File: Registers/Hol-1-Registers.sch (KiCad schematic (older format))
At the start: 26 parts, among them P1 DATA BUS, P2 REG-A-CTRL, P3 REG-B-CTRL, P4 REG-C-CTRL, P5 POWER, P6 CTRL-ALL, P7 REGISTER A LINK, P8 REGISTER B LINK, U1 74LS245, U2 74LS245, U3 74LS245, U4 74LS173, U5 74LS173, U6 74LS173, U7 74LS173, U8 74LS173, U9 74LS173

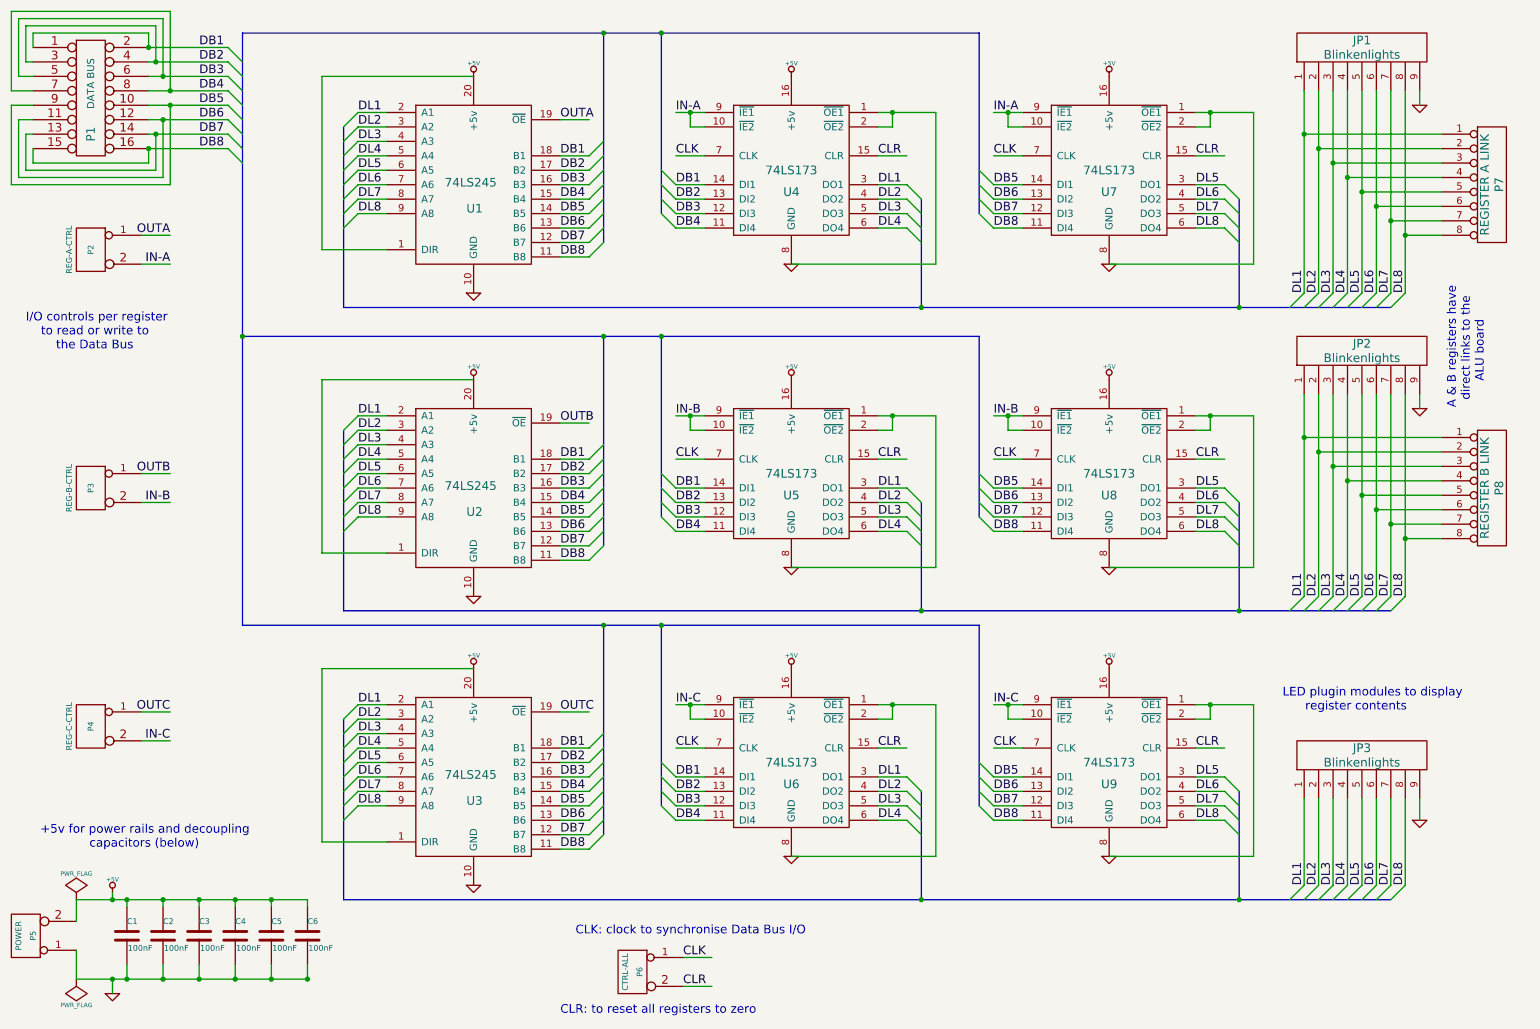
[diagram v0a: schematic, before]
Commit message: v1.3.2 corrected register net names
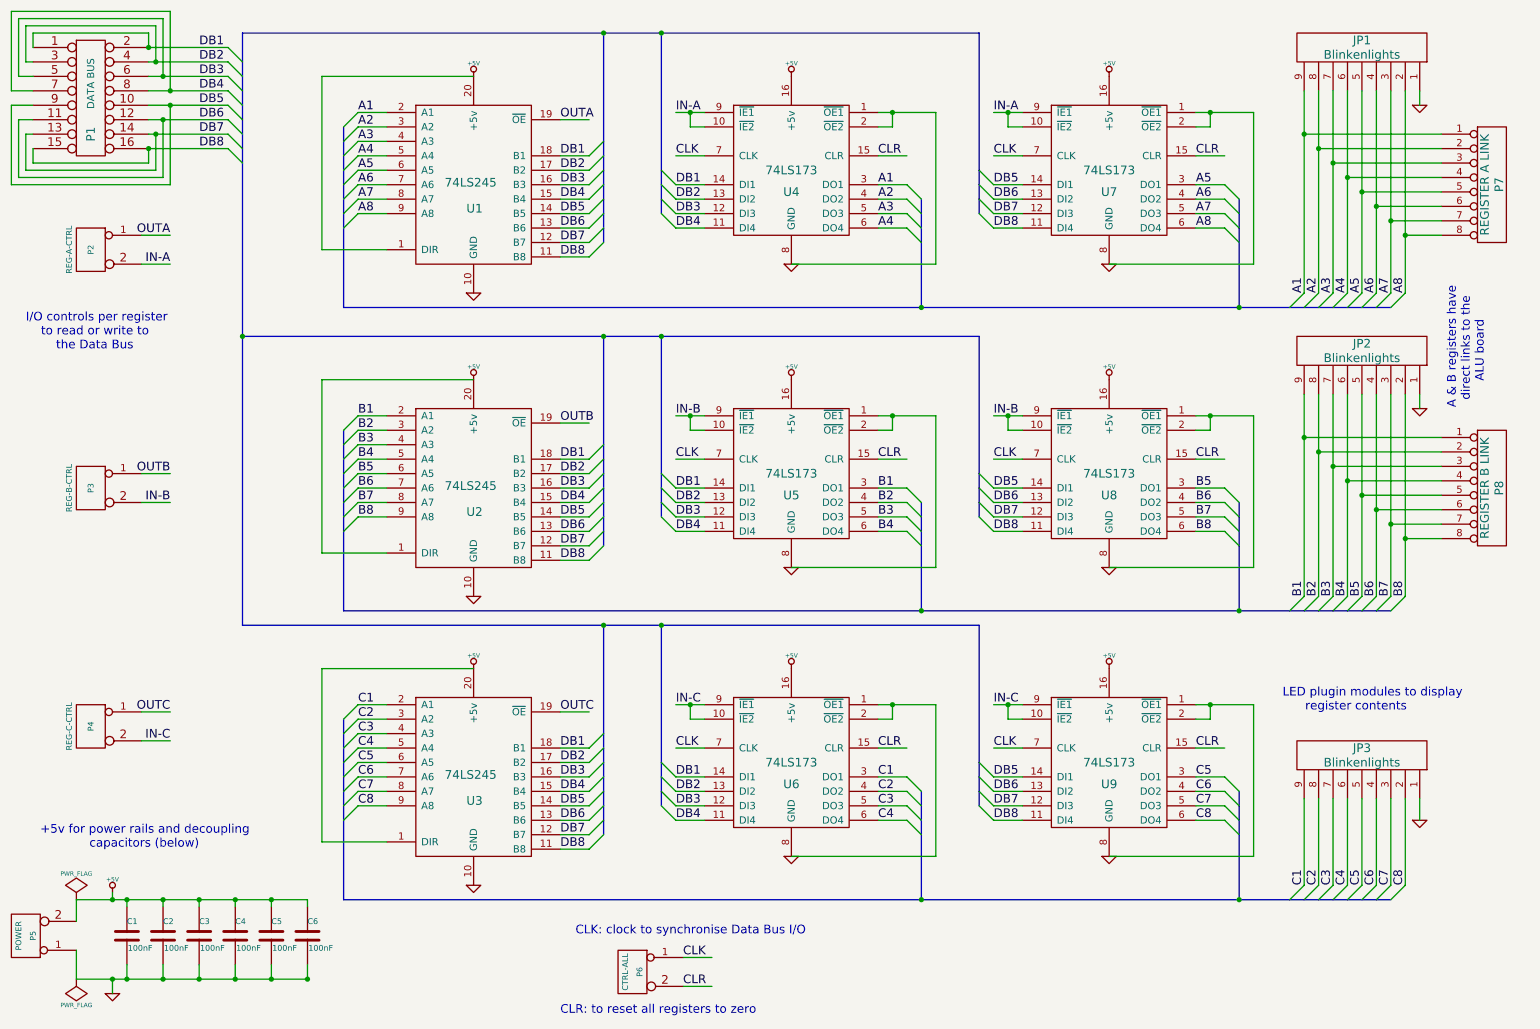
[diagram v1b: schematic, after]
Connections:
- net labels added: A1, A2, A3, A4, A5, A6, A7, A8, B1, B2, B3, B4, B5, B6, B7, B8, C1, C2, C3, C4, C5, C6, C7, C8
- net labels removed: DL1, DL2, DL3, DL4, DL5, DL6, DL7, DL8
- wire segments 275 -> 321

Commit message: v1.3.3 reduce dip footprints to correct length
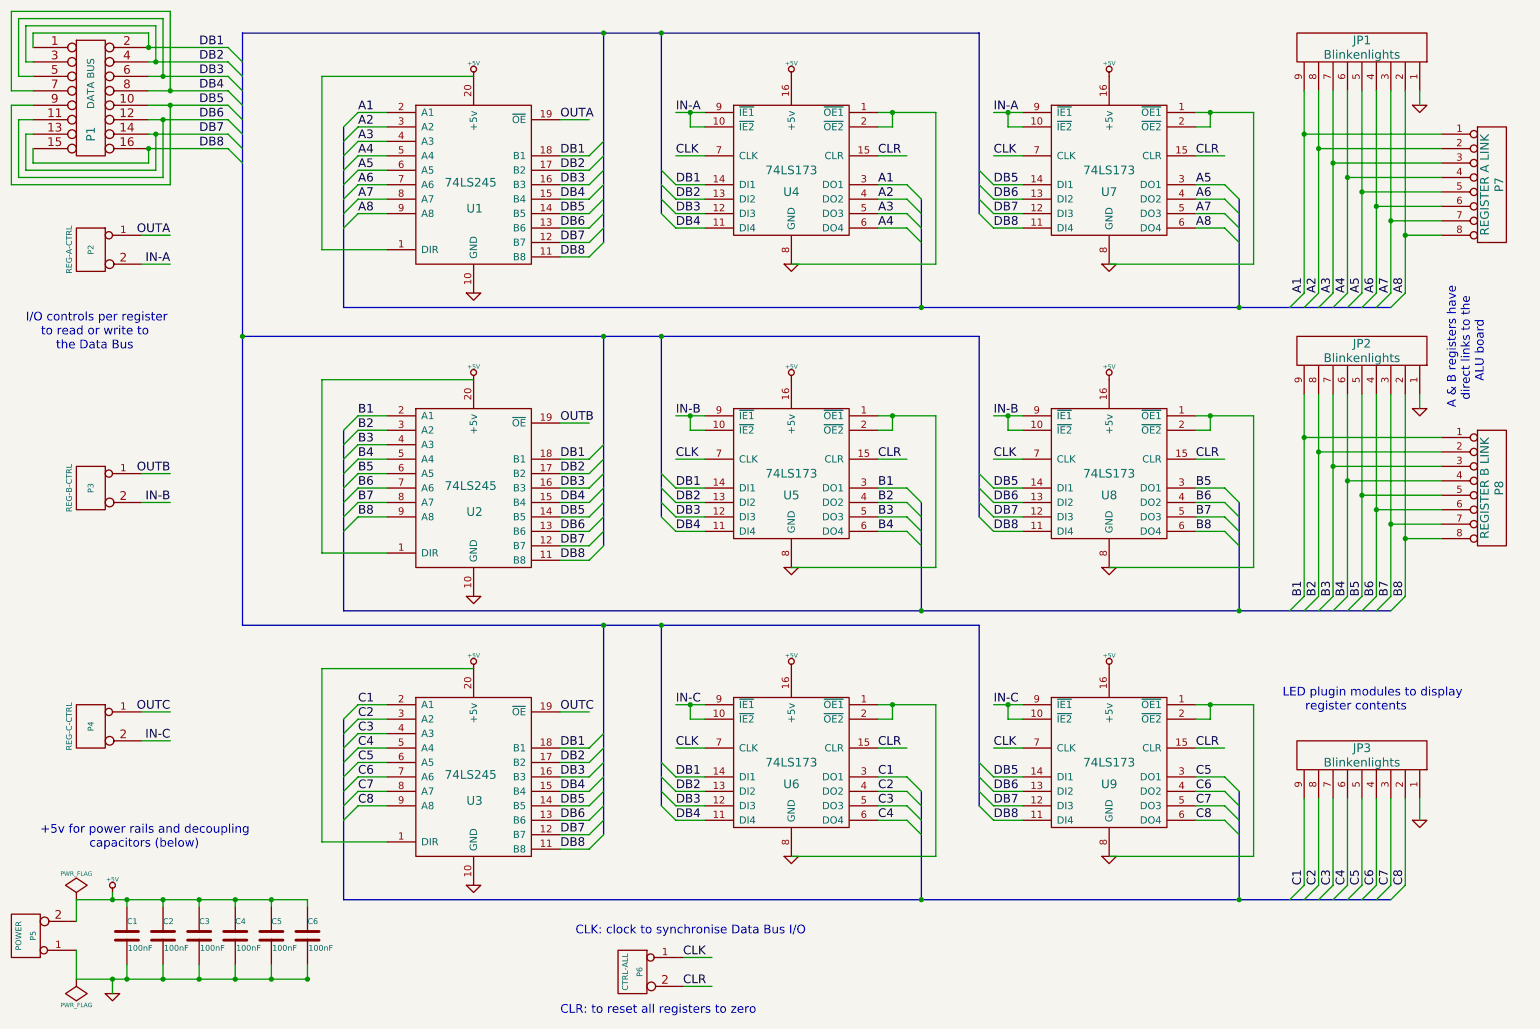
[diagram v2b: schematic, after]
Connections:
- wire segments 321 -> 275

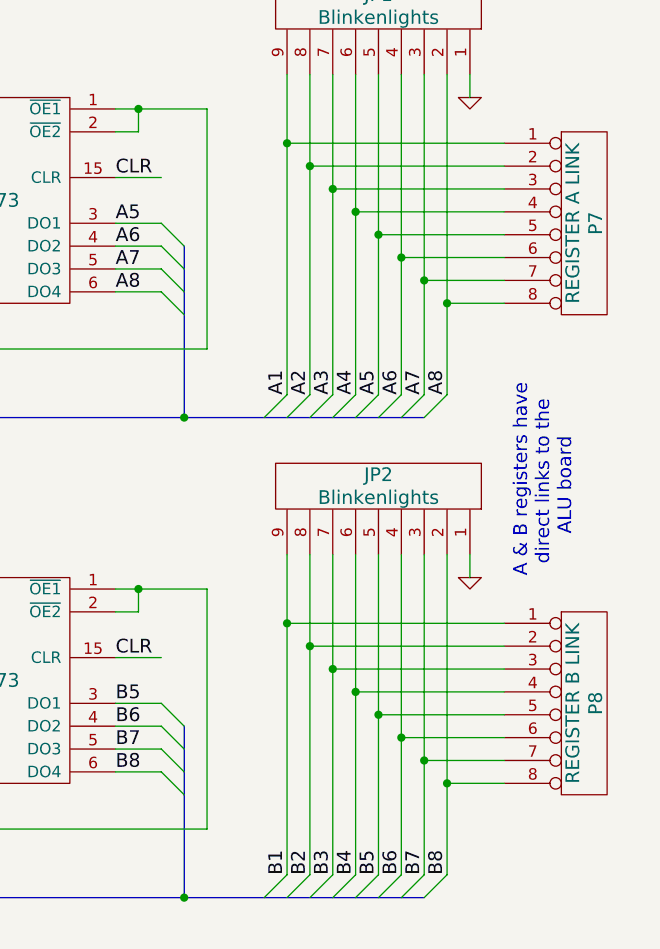
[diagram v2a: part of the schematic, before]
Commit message: v1.5.14 Registers: Re-numbered A & B ports. ALU to follow
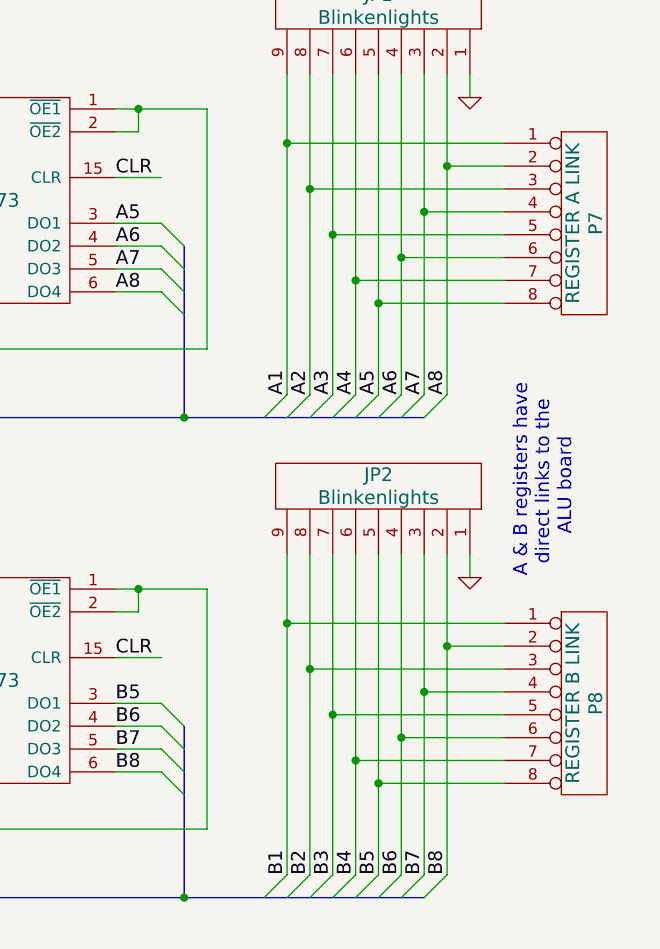
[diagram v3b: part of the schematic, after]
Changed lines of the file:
@@
 Sheet 1 1
 Title "Hol-1 8-bit CPU - Registers A, B & C board"
-Date "21 mar 2019"
+Date "18 jan 2020"
 Rev ""
 Comp "www.benningtons.net"
@@
 	10550 1550 9600 1550
 Connection ~ 9600 1550
-Connection ~ 9700 1650
-Connection ~ 9800 1750
-Connection ~ 9900 1850
-Connection ~ 10000 1950
-Connection ~ 10100 2050
-Connection ~ 10200 2150
-Connection ~ 10300 2250
 Wire Wire Line
 	800  1650 800  1750
@@
 	1    0    0    -1
 $EndComp
-Wire Wire Line
-	10550 1650 9700 1650
-Wire Wire Line
-	9800 1750 10550 1750
-Wire Wire Line
-	9900 1850 10550 1850
-Wire Wire Line
-	10000 1950 10550 1950
-Wire Wire Line
-	10100 2050 10550 2050
-Wire Wire Line
-	10200 2150 10550 2150
-Wire Wire Line
-	10300 2250 10550 2250
 Wire Wire Line
 	800  1350 650  1350
@@
 	-1   0    0    1
 $EndComp
-Wire Wire Line
-	10550 3650 9600 3650
 Connection ~ 9600 3650
-Connection ~ 9700 3750
-Connection ~ 9800 3850
-Connection ~ 9900 3950
-Connection ~ 10000 4050
-Connection ~ 10100 4150
-Connection ~ 10200 4250
-Connection ~ 10300 4350
 $Comp
 L GND #PWR018
@@
 	1    0    0    -1
 $EndComp
-Wire Wire Line
-	10550 3750 9700 3750
-Wire Wire Line
-	9800 3850 10550 3850
-Wire Wire Line
-	9900 3950 10550 3950
-Wire Wire Line
-	10000 4050 10550 4050
-Wire Wire Line
-	10100 4150 10550 4150
-Wire Wire Line
-	10200 4250 10550 4250
-Wire Wire Line
-	10300 4350 10550 4350
 Wire Wire Line
 	10400 3350 10400 3450
@@
 Text Notes 4450 7650 0    60   ~ 0
 CLR: to reset all registers to zero
+Connection ~ 10300 1650
+Wire Wire Line
+	10550 1650 10300 1650
+Connection ~ 9700 1750
+Wire Wire Line
+	10550 1750 9700 1750
+Connection ~ 10200 1850
+Wire Wire Line
+	10550 1850 10200 1850
+Connection ~ 9800 1950
+Connection ~ 10100 2050
+Connection ~ 9900 2150
+Connection ~ 10000 2250
+Wire Wire Line
+	10550 1950 9800 1950
+Wire Wire Line
+	10550 2050 10100 2050
+Wire Wire Line
+	10550 2150 9900 2150
+Wire Wire Line
+	10550 2250 10000 2250
+Connection ~ 10300 3750
+Connection ~ 9700 3850
+Connection ~ 10200 3950
+Connection ~ 9800 4050
+Connection ~ 10100 4150
+Connection ~ 9900 4250
+Connection ~ 10000 4350
+Wire Wire Line
+	10550 3650 9600 3650
+Wire Wire Line
+	10550 3750 10300 3750
+Wire Wire Line
+	10550 3850 9700 3850
+Wire Wire Line
+	10550 3950 10200 3950
+Wire Wire Line
+	10550 4050 9800 4050
+Wire Wire Line
+	10550 4150 10100 4150
+Wire Wire Line
+	10550 4250 9900 4250
+Wire Wire Line
+	10550 4350 10000 4350
 $EndSCHEMATC

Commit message: v1.5.19 upgraded to KiCad 5.0
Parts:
- C1, C2, C3, C4, C5, C6: symbol C -> benningtons:C
- JP1, JP2, JP3: symbol 9-PIN_HEADER -> benningtons:9-PIN_HEADER
- P1: symbol CONN_8X2 -> benningtons:CONN_8X2
- P2, P3, P4, P5, P6: symbol CONN_2 -> benningtons:CONN_2
- P7, P8: symbol CONN_8 -> benningtons:CONN_8
- U1, U2, U3: symbol 74LS245 -> benningtons:74LS245
- U4, U5, U6, U7, U8, U9: symbol 74LS173 -> benningtons:74LS173
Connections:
- wire segments 275 -> 321
